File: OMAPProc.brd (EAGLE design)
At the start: 44.5 x 23.2 mm, 42 parts, among them IC1 MIC5335-SPYMT, IC2 MIC5335-MGYMT, IC3 TXS0108ERGY, SW1 PWRON, SW2 RESET, SW3 USER

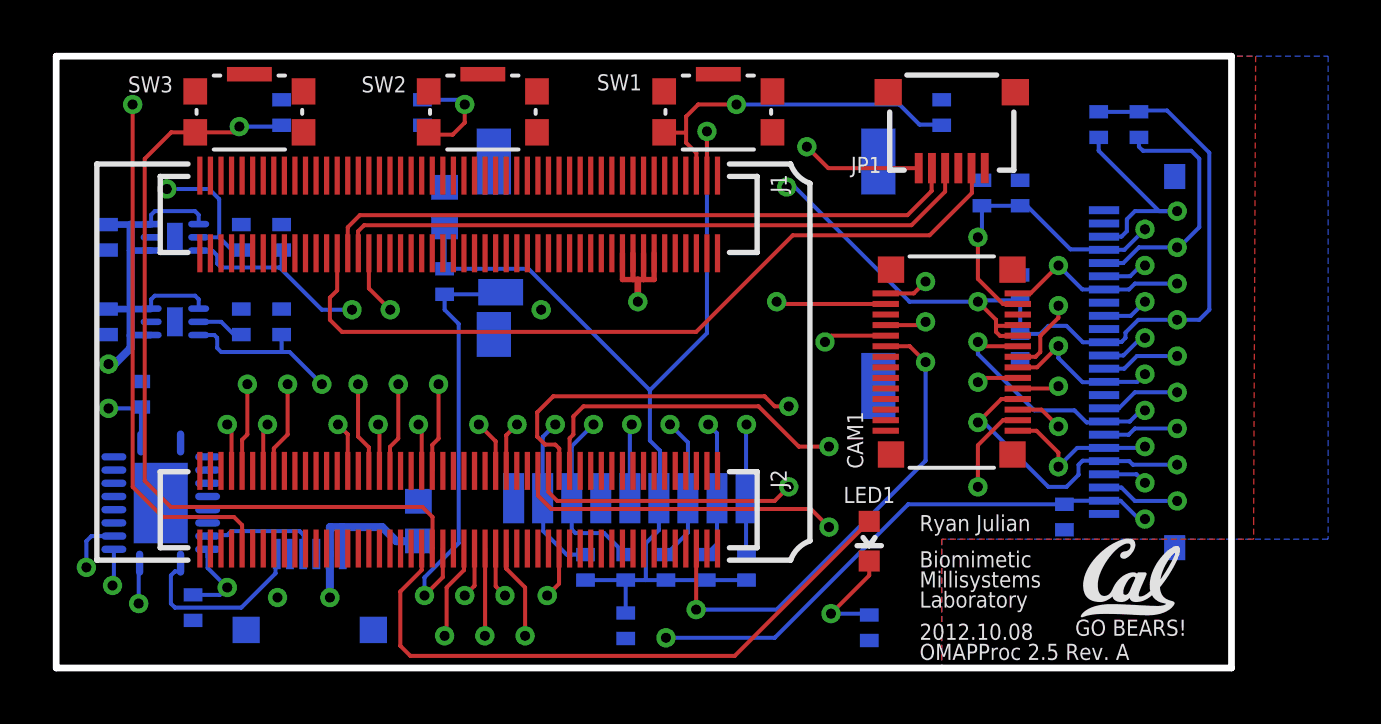
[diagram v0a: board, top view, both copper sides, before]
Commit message: Add USB connector
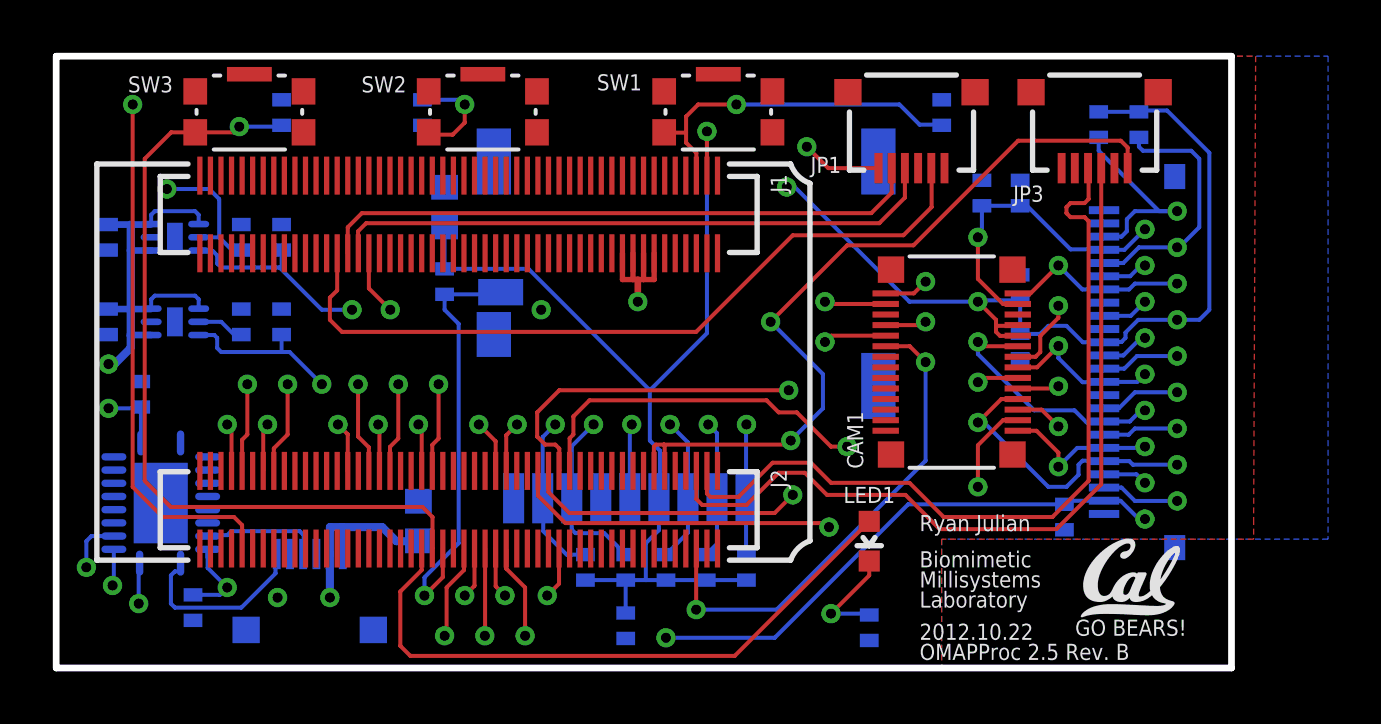
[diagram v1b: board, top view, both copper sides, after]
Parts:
- added JP3: USB, biomimetic:MOLEX_503480-0600
- moved JP1 1.52 mm to (32.4, 20.7)
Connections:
- new net USB1_D+: JP3.4, SOM1.J2.3
- new net USB1_D-: JP3.3, SOM1.J2.5
- new net USB1_VBUS: JP3.1, SOM1.J2.11, SOM1.J2.13
- net GND: now also JP3.6
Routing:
- net USB1_D-: track 0.00 -> 30.6 mm
- net USB1_D+: track 0.00 -> 30.5 mm
- net USB1_VBUS: track 0.00 -> 30.3 mm, vias 0 -> 2
- net CAM_MCLK: track 45.2 -> 43.4 mm
- net UARTA_CTS: track 25.4 -> 23.9 mm
- net UARTA_TX: track 24.5 -> 23.1 mm
- net UARTA_RX: track 24.6 -> 23.2 mm
- net UARTA_RTS: track 30.3 -> 29.0 mm
- net CAM_D7: track 36.7 -> 37.2 mm
- net CAM_D6: track 33.4 -> 33.9 mm
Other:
- board text added: "2012.10.22"
- board text added: "OMAPProc 2.5 Rev. B"
- board text removed: "2012.10.08"
- board text removed: "OMAPProc 2.5 Rev. A"
